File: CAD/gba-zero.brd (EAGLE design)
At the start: 130.7 x 72.9 mm, 59 parts, among them J1 SWTCHCRFT_3.5JACK5-JACK-SMD, P1 50_PIN_CON, P3 LINK_CONNECTOR, Q1 BSS138, U1 APX803, U2 NC7WZ16, U3 74LVC2G02, U4 74LVC3G04, U5 LM4875, U6 RPI-ZEROSMD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

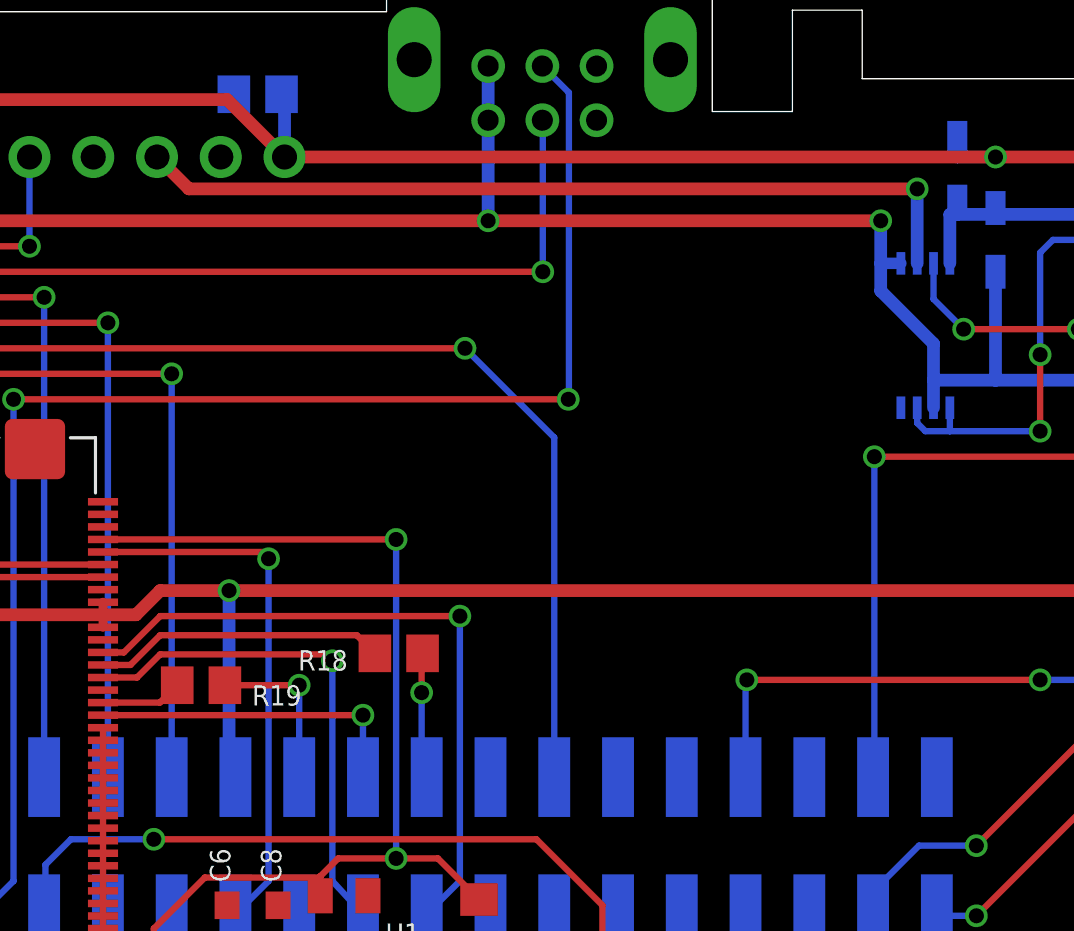
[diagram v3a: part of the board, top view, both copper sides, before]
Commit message: Added LBO to a GPIO5
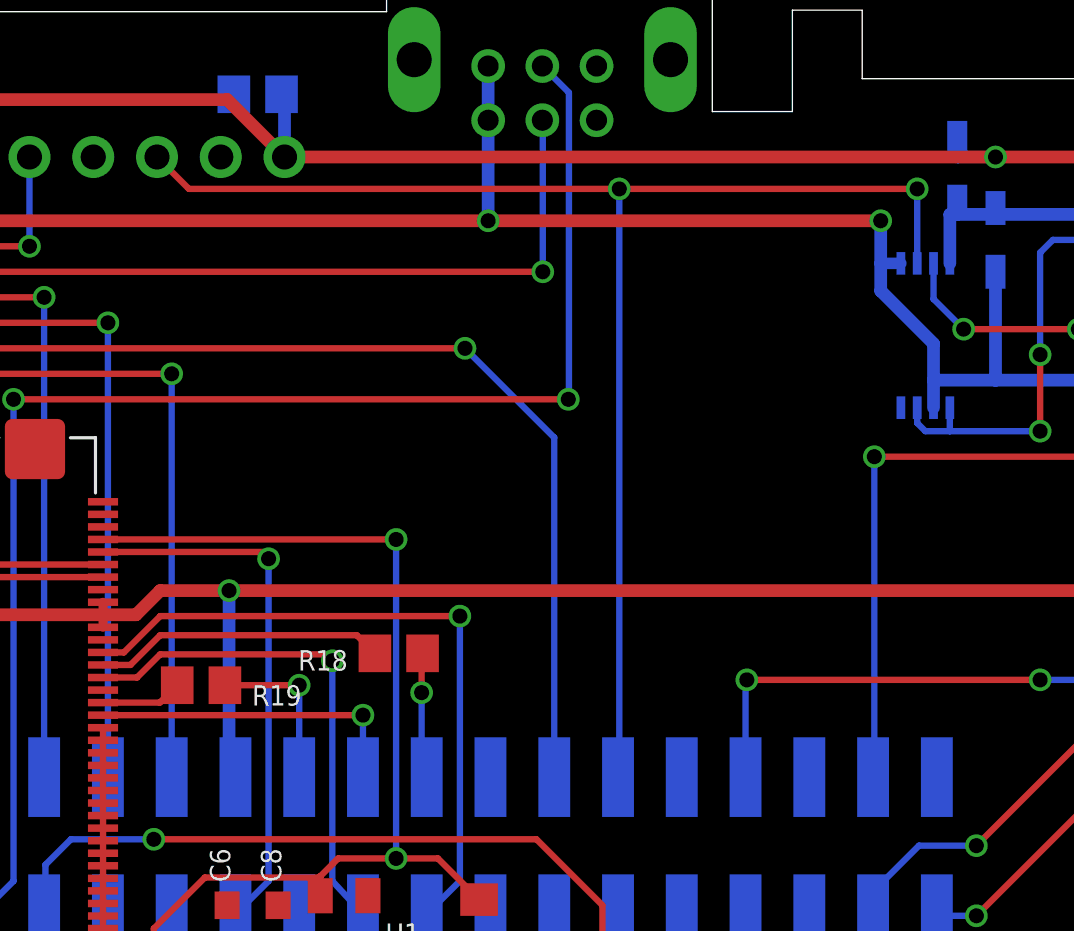
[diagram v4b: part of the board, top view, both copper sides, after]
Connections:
- net LBO: now also U6.29
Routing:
- net LBO: track 33.8 -> 57.2 mm, vias 1 -> 2
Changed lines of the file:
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@@
 <layer number="14" name="Route14" color="1" fill="6" visible="yes" active="yes"/>
 <layer number="15" name="Route15" color="4" fill="6" visible="yes" active="yes"/>
-<layer number="16" name="Bottom" color="1" fill="1" visible="yes" active="yes"/>
+<layer number="16" name="Bottom" color="1" fill="1" visible="no" active="yes"/>
 <layer number="17" name="Pads" color="2" fill="1" visible="yes" active="yes"/>
 <layer number="18" name="Vias" color="2" fill="1" visible="yes" active="yes"/>
@@
 <layer number="20" name="Dimension" color="15" fill="1" visible="yes" active="yes"/>
 <layer number="21" name="tPlace" color="14" fill="1" visible="yes" active="yes"/>
-<layer number="22" name="bPlace" color="13" fill="1" visible="yes" active="yes"/>
+<layer number="22" name="bPlace" color="13" fill="1" visible="no" active="yes"/>
 <layer number="23" name="tOrigins" color="15" fill="1" visible="yes" active="yes"/>
-<layer number="24" name="bOrigins" color="15" fill="1" visible="yes" active="yes"/>
+<layer number="24" name="bOrigins" color="15" fill="1" visible="no" active="yes"/>
 <layer number="25" name="tNames" color="7" fill="1" visible="yes" active="yes"/>
-<layer number="26" name="bNames" color="7" fill="1" visible="yes" active="yes"/>
+<layer number="26" name="bNames" color="7" fill="1" visible="no" active="yes"/>
 <layer number="27" name="tValues" color="7" fill="1" visible="yes" active="yes"/>
-<layer number="28" name="bValues" color="7" fill="1" visible="yes" active="yes"/>
+<layer number="28" name="bValues" color="7" fill="1" visible="no" active="yes"/>
 <layer number="29" name="tStop" color="7" fill="3" visible="yes" active="yes"/>
-<layer number="30" name="bStop" color="7" fill="6" visible="yes" active="yes"/>
+<layer number="30" name="bStop" color="7" fill="6" visible="no" active="yes"/>
 <layer number="31" name="tCream" color="7" fill="4" visible="yes" active="yes"/>
-<layer number="32" name="bCream" color="7" fill="5" visible="yes" active="yes"/>
+<layer number="32" name="bCream" color="7" fill="5" visible="no" active="yes"/>
 <layer number="33" name="tFinish" color="6" fill="3" visible="yes" active="yes"/>
-<layer number="34" name="bFinish" color="6" fill="6" visible="yes" active="yes"/>
+<layer number="34" name="bFinish" color="6" fill="6" visible="no" active="yes"/>
 <layer number="35" name="tGlue" color="7" fill="4" visible="yes" active="yes"/>
-<layer number="36" name="bGlue" color="7" fill="5" visible="yes" active="yes"/>
+<layer number="36" name="bGlue" color="7" fill="5" visible="no" active="yes"/>
 <layer number="37" name="tTest" color="7" fill="1" visible="yes" active="yes"/>
-<layer number="38" name="bTest" color="7" fill="1" visible="yes" active="yes"/>
+<layer number="38" name="bTest" color="7" fill="1" visible="no" active="yes"/>
 <layer number="39" name="tKeepout" color="4" fill="11" visible="yes" active="yes"/>
-<layer number="40" name="bKeepout" color="1" fill="11" visible="yes" active="yes"/>
+<layer number="40" name="bKeepout" color="1" fill="11" visible="no" active="yes"/>
 <layer number="41" name="tRestrict" color="4" fill="10" visible="yes" active="yes"/>
-<layer number="42" name="bRestrict" color="1" fill="10" visible="yes" active="yes"/>
+<layer number="42" name="bRestrict" color="1" fill="10" visible="no" active="yes"/>
 <layer number="43" name="vRestrict" color="2" fill="10" visible="yes" active="yes"/>
 <layer number="44" name="Drills" color="7" fill="1" visible="yes" active="yes"/>
@@
 <layer number="50" name="dxf" color="7" fill="1" visible="yes" active="yes"/>
 <layer number="51" name="tDocu" color="7" fill="1" visible="yes" active="yes"/>
-<layer number="52" name="bDocu" color="7" fill="1" visible="yes" active="yes"/>
+<layer number="52" name="bDocu" color="7" fill="1" visible="no" active="yes"/>
 <layer number="53" name="tGND_GNDA" color="7" fill="9" visible="no" active="no"/>
 <layer number="54" name="bGND_GNDA" color="1" fill="9" visible="no" active="no"/>
@@
 <layer number="57" name="tCAD" color="7" fill="1" visible="no" active="no"/>
 <layer number="59" name="tCarbon" color="7" fill="1" visible="yes" active="yes"/>
-<layer number="60" name="bCarbon" color="7" fill="1" visible="yes" active="yes"/>
+<layer number="60" name="bCarbon" color="7" fill="1" visible="no" active="yes"/>
 <layer number="90" name="Modules" color="7" fill="1" visible="no" active="no"/>
 <layer number="91" name="Nets" color="2" fill="1" visible="no" active="no"/>
@@
 <layer number="122" name="_bsilk" color="7" fill="1" visible="yes" active="yes"/>
 <layer number="123" name="tTestmark" color="7" fill="1" visible="yes" active="yes"/>
-<layer number="124" name="bTestmark" color="7" fill="1" visible="yes" active="yes"/>
+<layer number="124" name="bTestmark" color="7" fill="1" visible="no" active="yes"/>
 <layer number="125" name="_tNames" color="7" fill="1" visible="yes" active="yes"/>
-<layer number="126" name="_bNames" color="7" fill="1" visible="yes" active="yes"/>
+<layer number="126" name="_bNames" color="7" fill="1" visible="no" active="yes"/>
 <layer number="127" name="_tValues" color="7" fill="1" visible="yes" active="yes"/>
-<layer number="128" name="_bValues" color="7" fill="1" visible="yes" active="yes"/>
+<layer number="128" name="_bValues" color="7" fill="1" visible="no" active="yes"/>
 <layer number="129" name="Mask" color="7" fill="1" visible="yes" active="yes"/>
 <layer number="130" name="mbStop" color="7" fill="1" visible="yes" active="yes"/>
 <layer number="131" name="tAdjust" color="7" fill="1" visible="yes" active="yes"/>
-<layer number="132" name="bAdjust" color="7" fill="1" visible="yes" active="yes"/>
+<layer number="132" name="bAdjust" color="7" fill="1" visible="no" active="yes"/>
 <layer number="133" name="mtFinish" color="7" fill="1" visible="yes" active="yes"/>
-<layer number="134" name="mbFinish" color="7" fill="1" visible="yes" active="yes"/>
+<layer number="134" name="mbFinish" color="7" fill="1" visible="no" active="yes"/>
 <layer number="135" name="mtGlue" color="7" fill="1" visible="yes" active="yes"/>
-<layer number="136" name="mbGlue" color="7" fill="1" visible="yes" active="yes"/>
+<layer number="136" name="mbGlue" color="7" fill="1" visible="no" active="yes"/>
 <layer number="137" name="mtTest" color="7" fill="1" visible="yes" active="yes"/>
-<layer number="138" name="mbTest" color="7" fill="1" visible="yes" active="yes"/>
+<layer number="138" name="mbTest" color="7" fill="1" visible="no" active="yes"/>
 <layer number="139" name="mtKeepout" color="7" fill="1" visible="yes" active="yes"/>
-<layer number="140" name="mbKeepout" color="7" fill="1" visible="yes" active="yes"/>
+<layer number="140" name="mbKeepout" color="7" fill="1" visible="no" active="yes"/>
 <layer number="141" name="mtRestrict" color="7" fill="1" visible="yes" active="yes"/>
-<layer number="142" name="mbRestrict" color="7" fill="1" visible="yes" active="yes"/>
+<layer number="142" name="mbRestrict" color="7" fill="1" visible="no" active="yes"/>
 <layer number="143" name="mvRestrict" color="7" fill="1" visible="yes" active="yes"/>
 <layer number="144" name="Drill_legend" color="7" fill="1" visible="yes" active="yes"/>
@@
 <layer number="150" name="Notes" color="7" fill="1" visible="yes" active="yes"/>
 <layer number="151" name="HeatSink" color="7" fill="1" visible="yes" active="yes"/>
-<layer number="152" name="_bDocu" color="7" fill="1" visible="yes" active="yes"/>
+<layer number="152" name="_bDocu" color="7" fill="1" visible="no" active="yes"/>
 <layer number="153" name="FabDoc1" color="6" fill="1" visible="no" active="no"/>
 <layer number="154" name="FabDoc2" color="2" fill="1" visible="no" active="no"/>
@@
 <contactref element="U3" pad="6"/>
 <contactref element="U7" pad="LBO"/>
-<wire x1="90.353" y1="61.803" x2="90.353" y2="64.77" width="0.508" layer="16"/>
+<wire x1="90.353" y1="61.803" x2="90.353" y2="64.77" width="0.254" layer="16"/>
 <via x="90.353" y="64.77" extent="1-16" drill="0.6" shape="square"/>
-<wire x1="90.353" y1="64.77" x2="61.341" y2="64.77" width="0.508" layer="1"/>
-<wire x1="61.341" y1="64.77" x2="60.071" y2="66.04" width="0.508" layer="1"/>
+<wire x1="90.353" y1="64.77" x2="78.486" y2="64.77" width="0.254" layer="1"/>
+<wire x1="78.486" y1="64.77" x2="61.341" y2="64.77" width="0.254" layer="1"/>
+<wire x1="61.341" y1="64.77" x2="60.071" y2="66.04" width="0.254" layer="1"/>
+<contactref element="U6" pad="29"/>
+<wire x1="78.4352" y1="41.3385" x2="78.486" y2="41.3893" width="0.254" layer="16"/>
+<wire x1="78.486" y1="41.3893" x2="78.486" y2="64.77" width="0.254" layer="16"/>
+<via x="78.486" y="64.77" extent="1-16" drill="0.6" shape="square"/>
 </signal>
 <signal name="N$18">

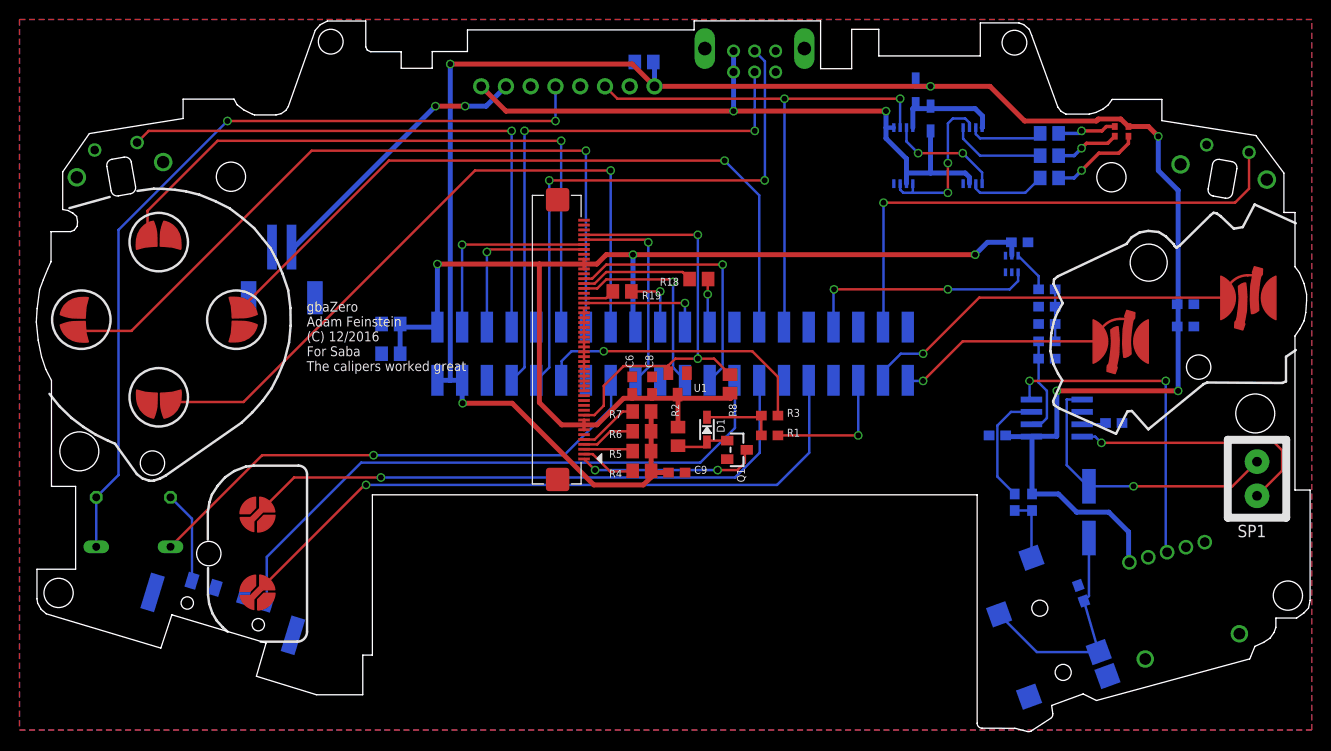
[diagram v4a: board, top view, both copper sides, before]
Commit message: Moved RPi Zero up a little
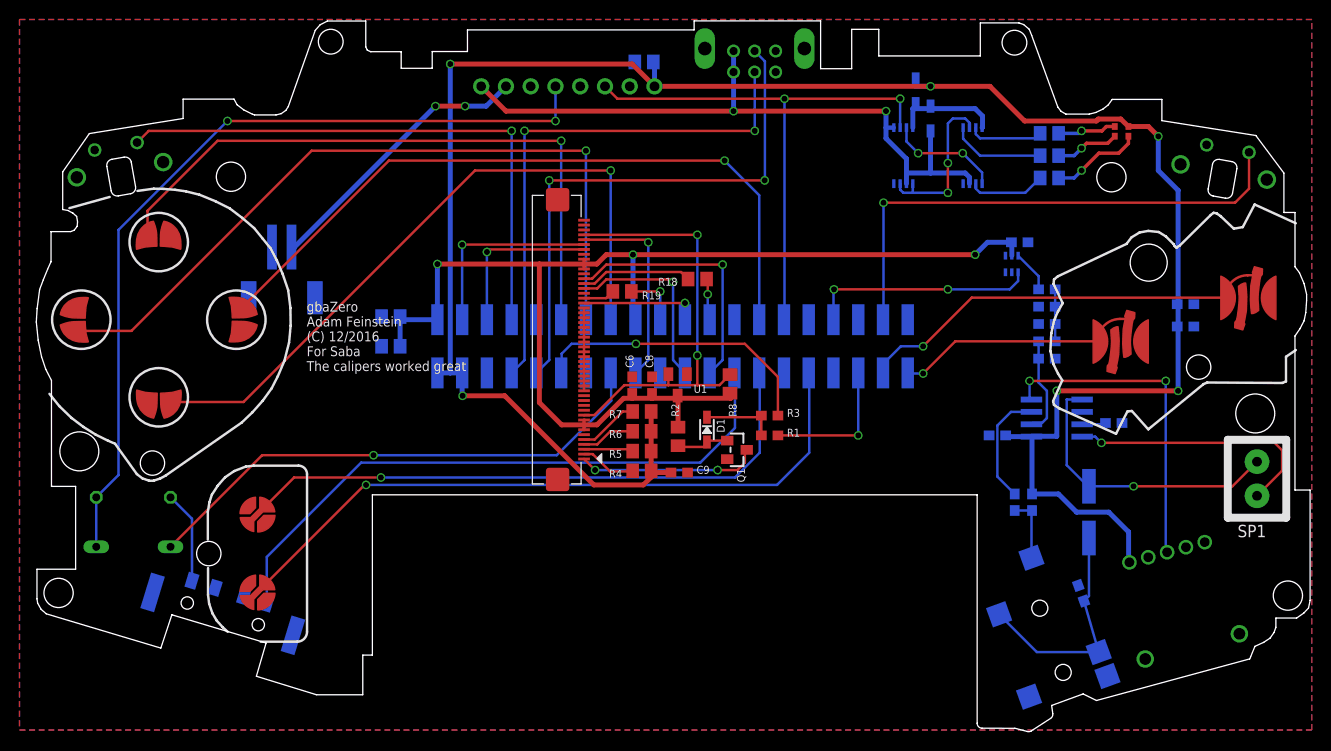
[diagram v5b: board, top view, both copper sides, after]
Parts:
- moved C11 0.76 mm to (38.1, 39.4)
- moved C12 0.76 mm to (38.1, 42.4)
- moved U6 0.76 mm to (67.0, 39.4)
- moved C9 0.25 mm to (67.7, 26.4)
- moved R18 0.15 mm to (69.5, 46.3)
- moved U1 0.10 mm to (67.5, 35.4)
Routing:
- net 3.3V: track 125.0 -> 123.4 mm
- net TXD: track 55.8 -> 55.0 mm
- net TFT_CS_3V: track 27.2 -> 26.5 mm
- net PWR_SW_SEN: track 63.2 -> 64.0 mm
- net BTN_STR: track 61.6 -> 62.4 mm
- net BTN_SEL: track 70.1 -> 70.8 mm
- net BTN_R: track 74.4 -> 73.7 mm
- net BKLT: track 13.9 -> 14.7 mm
- net RT_INT: track 21.6 -> 20.8 mm
- net TFT_DC_3V: track 20.2 -> 19.4 mm
- net SDA: track 21.0 -> 20.2 mm
- net SCL: track 17.9 -> 17.2 mm
- net RXD: track 56.9 -> 56.1 mm
- net MOSI_3V: track 6.62 -> 5.86 mm
- net MISO: track 12.8 -> 12.1 mm
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
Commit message: Replaced 0805s with 0603s Fattened power traces
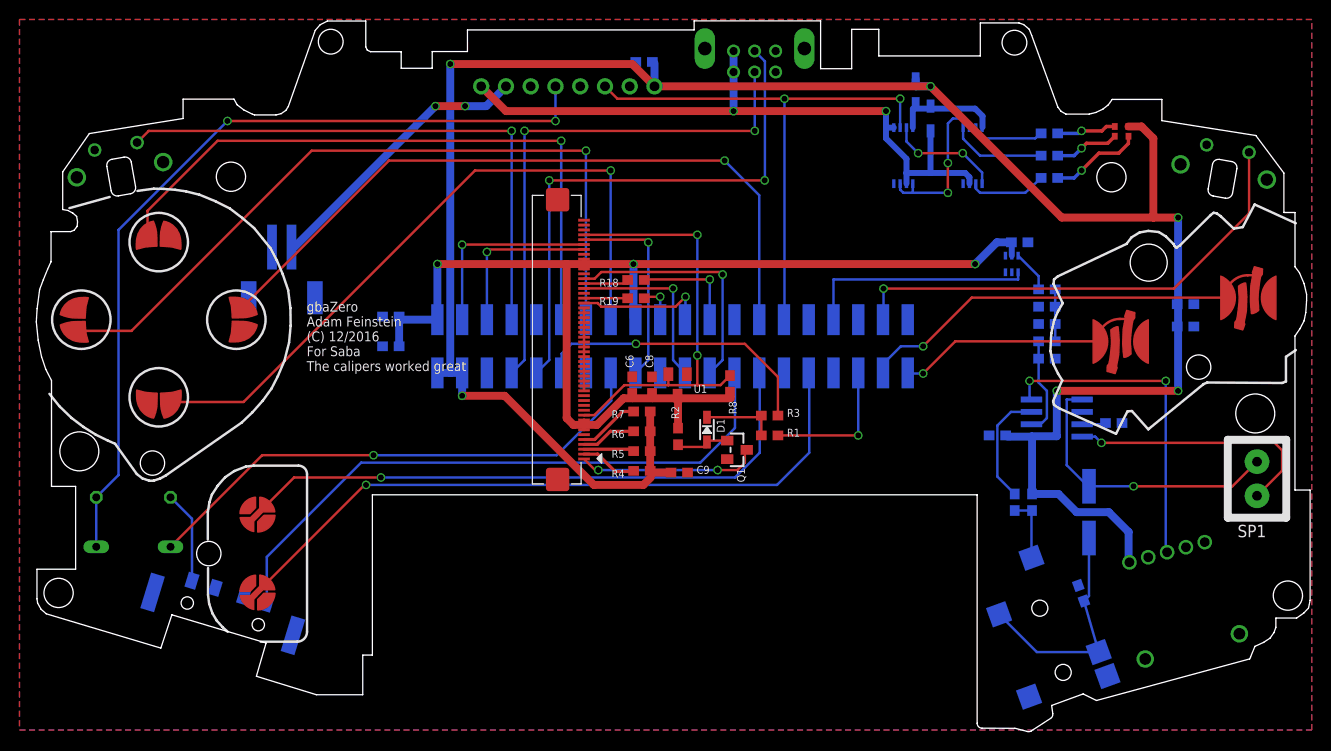
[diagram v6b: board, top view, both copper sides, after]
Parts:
- C11, C12, C14, R14, R15, R16, R18, R19, R2, R4, R5, R6, R7, R8: device microbuilder:0805 -> microbuilder:0603
- moved R18 6.30 mm to (63.2, 46.2)
- moved R19 1.58 mm to (63.2, 44.3)
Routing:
- net +5V: track 219.8 -> 227.6 mm
- net SCLK: track 11.5 -> 4.85 mm
- net SCLK_3V: track 4.46 -> 10.9 mm
- net BTN_RS: track 53.9 -> 50.2 mm
- net 3.3V: track 123.4 -> 120.8 mm
- net MOSI_3V: track 5.86 -> 4.14 mm
- net MISO: track 12.1 -> 13.4 mm
- net MOSI: track 3.24 -> 4.48 mm
- net TFT_CS_3V: track 26.5 -> 25.2 mm
- net TFT_DC_3V: track 19.4 -> 18.3 mm
- net AUD_PWM: track 23.3 -> 23.8 mm, vias 2 -> 0
